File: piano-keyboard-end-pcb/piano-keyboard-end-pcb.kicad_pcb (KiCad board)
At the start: 2 copper layers, 41.1 x 82 mm, 24 parts, among them J1 Conn_01x03_Male, J2 Conn_01x01_Male, J3 Conn_01x02_Male, J4 Conn_01x02_Male, J5 Conn_01x05_Female, J6 AudioJack2, SW1 SW_Push, SW2 SW_Push, SW3 SW_Push, SW4 SW_Push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

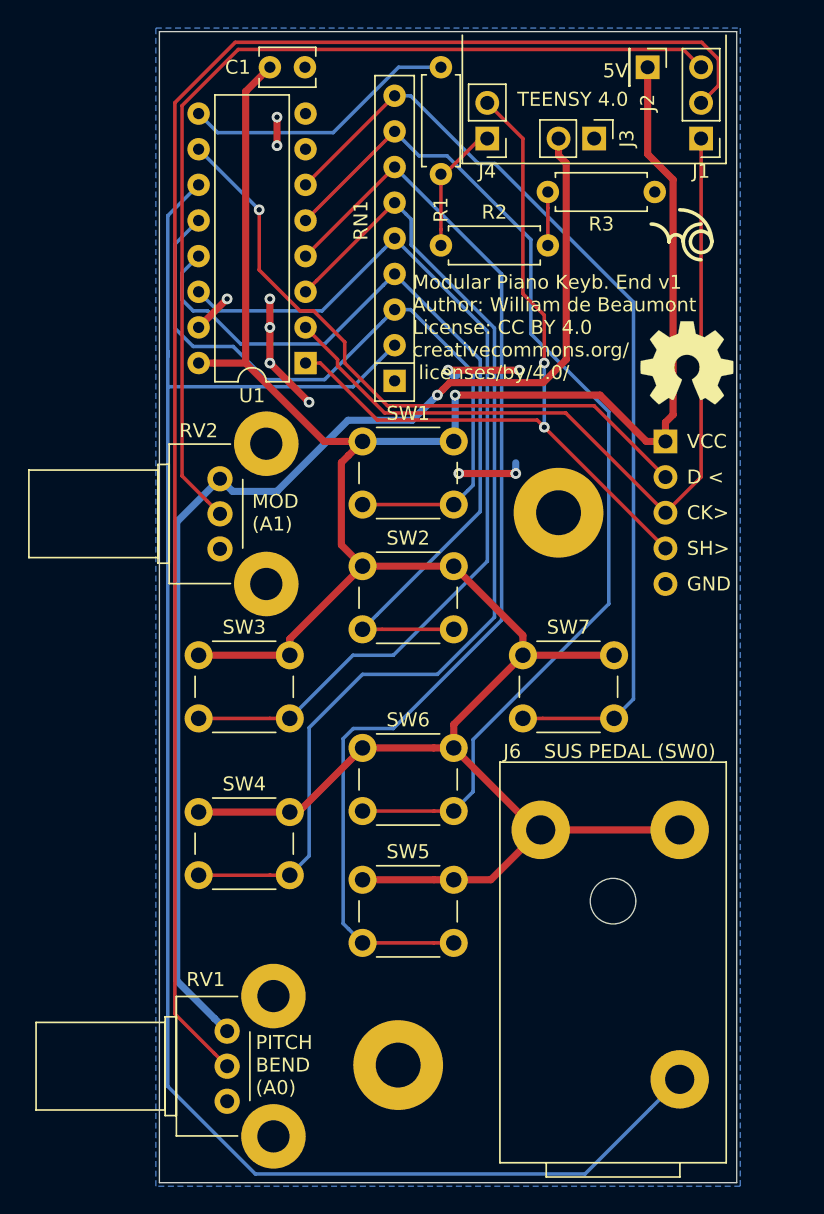
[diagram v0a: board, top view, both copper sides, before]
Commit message: move mod pot right so it aligns with edge and pitch bend pot
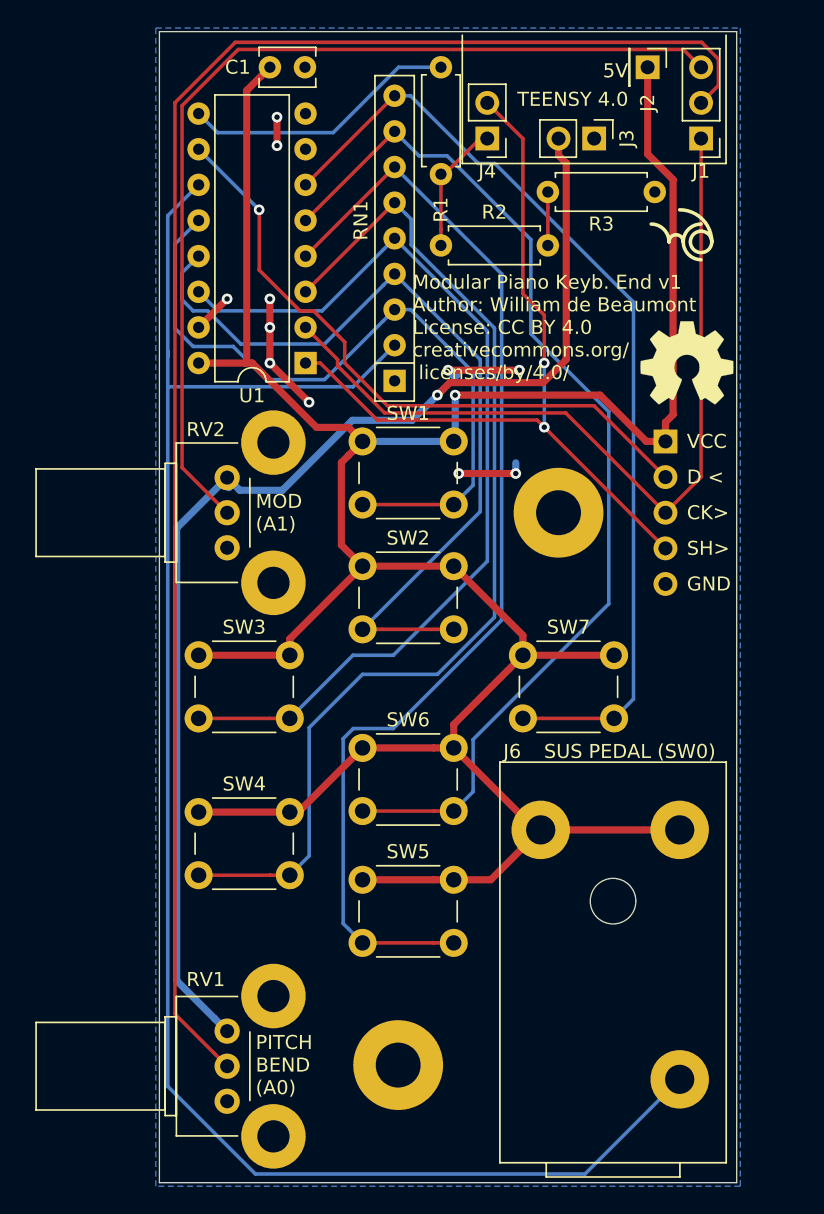
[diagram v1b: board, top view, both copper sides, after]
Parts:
- moved RV2 0.52 mm to (79.2, 68.6)
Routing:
- net +3V3: track 87.1 -> 87.7 mm
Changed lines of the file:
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@@
     (thickness 1.6)
     (drawings 23)
-    (tracks 233)
+    (tracks 236)
     (zones 0)
     (modules 24)
@@
   )
   (module Potentiometer_THT:Potentiometer_Bourns_PTV09A-2_Single_Horizontal (layer F.Cu)
-    (at 78.74 68.7 180)
+    (at 79.25 68.62 180)
     (descr "Potentiometer, horizontal, Bourns PTV09A-2 Single, http://www.bourns.com/docs/Product-Datasheets/ptv09.pdf")
     (tags "Potentiometer horizontal Bourns PTV09A-2 Single")
@@
     (effects (font (size 1 1) (thickness 0.15)) (justify left))
   )
-  (gr_text "MOD\n(A1)" (at 81.026 71.12) (layer F.SilkS)
+  (gr_text "MOD\n(A1)" (at 81.28 71.12) (layer F.SilkS)
     (effects (font (size 1 1) (thickness 0.15)) (justify left))
   )
@@
   (segment (start 82.296 57.912) (end 82.296 55.88) (width 0.508) (layer F.Cu) (net 1))
   (segment (start 95.4 66.04) (end 88.9 66.04) (width 0.508) (layer B.Cu) (net 2))
-  (segment (start 78.34737 60.452) (end 77.216 60.452) (width 0.508) (layer F.Cu) (net 2))
-  (segment (start 80.567842 60.452) (end 78.34737 60.452) (width 0.508) (layer F.Cu) (net 2))
-  (segment (start 86.155842 66.04) (end 80.567842 60.452) (width 0.508) (layer F.Cu) (net 2))
-  (segment (start 88.9 66.04) (end 86.155842 66.04) (width 0.508) (layer F.Cu) (net 2))
-  (segment (start 80.567842 41.098158) (end 82.296 39.37) (width 0.508) (layer F.Cu) (net 2))
-  (segment (start 80.567842 60.452) (end 80.567842 41.098158) (width 0.508) (layer F.Cu) (net 2))
   (segment (start 100.33 81.28) (end 106.83 81.28) (width 0.508) (layer F.Cu) (net 2))
   (segment (start 95.4 86.21) (end 100.33 81.28) (width 0.508) (layer F.Cu) (net 2))
@@
   (segment (start 109.22 45.562158) (end 111.036001 47.378159) (width 0.508) (layer F.Cu) (net 2))
   (segment (start 109.22 39.37) (end 109.22 45.562158) (width 0.508) (layer F.Cu) (net 2))
-  (segment (start 77.840001 70.300001) (end 78.74 71.2) (width 0.254) (layer F.Cu) (net 3))
-  (segment (start 76.034999 68.494999) (end 77.840001 70.300001) (width 0.254) (layer F.Cu) (net 3))
-  (segment (start 76.034999 42.105119) (end 76.034999 68.494999) (width 0.254) (layer F.Cu) (net 3))
+  (segment (start 78.34737 60.452) (end 77.216 60.452) (width 0.508) (layer F.Cu) (net 2))
+  (segment (start 85.625843 65.040001) (end 81.037842 60.452) (width 0.508) (layer F.Cu) (net 2))
+  (segment (start 87.900001 65.040001) (end 85.625843 65.040001) (width 0.508) (layer F.Cu) (net 2))
+  (segment (start 88.9 66.04) (end 87.900001 65.040001) (width 0.508) (layer F.Cu) (net 2))
+  (segment (start 80.644999 41.021001) (end 80.644999 60.325001) (width 0.508) (layer F.Cu) (net 2))
+  (segment (start 80.644999 60.325001) (end 80.518 60.452) (width 0.508) (layer F.Cu) (net 2))
+  (segment (start 82.296 39.37) (end 80.644999 41.021001) (width 0.508) (layer F.Cu) (net 2))
+  (segment (start 81.037842 60.452) (end 80.518 60.452) (width 0.508) (layer F.Cu) (net 2))
+  (segment (start 80.518 60.452) (end 78.34737 60.452) (width 0.508) (layer F.Cu) (net 2))
   (segment (start 111.76 38.1) (end 80.040118 38.1) (width 0.254) (layer F.Cu) (net 3))
   (segment (start 80.040118 38.1) (end 76.034999 42.105119) (width 0.254) (layer F.Cu) (net 3))
   (segment (start 113.03 39.37) (end 111.76 38.1) (width 0.254) (layer F.Cu) (net 3))
+  (segment (start 76.034999 67.904999) (end 79.25 71.12) (width 0.254) (layer F.Cu) (net 3))
+  (segment (start 76.034999 42.105119) (end 76.034999 67.904999) (width 0.254) (layer F.Cu) (net 3))
   (segment (start 75.526989 106.846989) (end 78.350001 109.670001) (width 0.254) (layer F.Cu) (net 4))
   (segment (start 75.526989 41.894695) (end 75.526989 106.846989) (width 0.254) (layer F.Cu) (net 4))
@@
   (segment (start 103.378 64.008) (end 110.49 71.12) (width 0.254) (layer F.Cu) (net 5))
   (segment (start 90.467764 64.008) (end 103.378 64.008) (width 0.254) (layer F.Cu) (net 5))
-  (segment (start 79.639999 69.599999) (end 78.74 68.7) (width 0.508) (layer B.Cu) (net 6))
-  (segment (start 87.863843 64.531999) (end 82.795843 69.599999) (width 0.508) (layer B.Cu) (net 6))
-  (segment (start 82.795843 69.599999) (end 79.639999 69.599999) (width 0.508) (layer B.Cu) (net 6))
-  (segment (start 75.653991 104.473991) (end 78.350001 107.170001) (width 0.508) (layer B.Cu) (net 6))
-  (segment (start 78.350001 107.170001) (end 79.25 108.07) (width 0.508) (layer B.Cu) (net 6))
-  (segment (start 75.653991 71.786009) (end 75.653991 104.473991) (width 0.508) (layer B.Cu) (net 6))
-  (segment (start 78.74 68.7) (end 75.653991 71.786009) (width 0.508) (layer B.Cu) (net 6))
   (via (at 94.234 62.738) (size 0.762) (drill 0.381) (layers F.Cu B.Cu) (net 6))
   (segment (start 94.218001 62.753999) (end 94.234 62.738) (width 0.508) (layer B.Cu) (net 6))
@@
   (segment (start 95.123001 61.848999) (end 94.614999 62.357001) (width 0.508) (layer F.Cu) (net 6))
   (segment (start 101.772723 61.848999) (end 95.123001 61.848999) (width 0.508) (layer F.Cu) (net 6))
-  (segment (start 92.440001 64.531999) (end 94.234 62.738) (width 0.508) (layer B.Cu) (net 6))
-  (segment (start 87.863843 64.531999) (end 92.440001 64.531999) (width 0.508) (layer B.Cu) (net 6))
   (segment (start 103.416001 60.205721) (end 101.772723 61.848999) (width 0.508) (layer F.Cu) (net 6))
   (segment (start 103.416001 46.198082) (end 103.416001 60.205721) (width 0.508) (layer F.Cu) (net 6))
   (segment (start 102.87 45.652081) (end 103.416001 46.198082) (width 0.508) (layer F.Cu) (net 6))
   (segment (start 102.87 44.45) (end 102.87 45.652081) (width 0.508) (layer F.Cu) (net 6))
+  (segment (start 78.350001 107.170001) (end 79.25 108.07) (width 0.508) (layer B.Cu) (net 6))
+  (segment (start 75.653991 104.473991) (end 78.350001 107.170001) (width 0.508) (layer B.Cu) (net 6))
+  (segment (start 79.382 69.342) (end 78.74 68.7) (width 0.508) (layer B.Cu) (net 6))
+  (segment (start 94.234 62.738) (end 92.440001 64.531999) (width 0.508) (layer B.Cu) (net 6))
+  (segment (start 75.653991 72.216009) (end 75.653991 104.473991) (width 0.508) (layer B.Cu) (net 6))
+  (segment (start 79.25 68.62) (end 75.653991 72.216009) (width 0.508) (layer B.Cu) (net 6))
+  (segment (start 80.149999 69.519999) (end 79.25 68.62) (width 0.508) (layer B.Cu) (net 6))
+  (segment (start 83.188159 69.519999) (end 80.149999 69.519999) (width 0.508) (layer B.Cu) (net 6))
+  (segment (start 88.176159 64.531999) (end 83.188159 69.519999) (width 0.508) (layer B.Cu) (net 6))
+  (segment (start 92.440001 64.531999) (end 88.176159 64.531999) (width 0.508) (layer B.Cu) (net 6))
   (segment (start 100.33 44.45) (end 97.79 41.91) (width 0.254) (layer F.Cu) (net 7))
   (segment (start 89.95401 64.51601) (end 85.89 60.452) (width 0.254) (layer F.Cu) (net 7))

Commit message: move pitch bend pot up slightly to align with 10mil grid
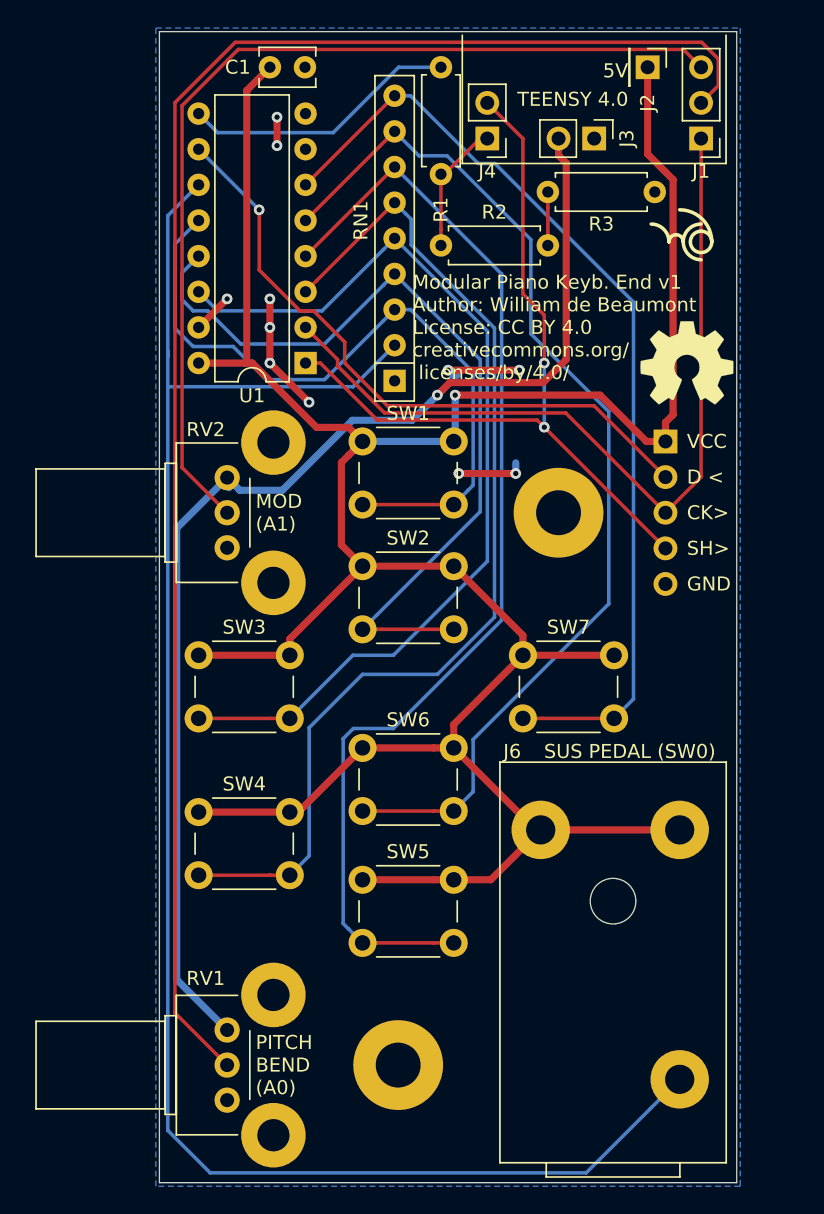
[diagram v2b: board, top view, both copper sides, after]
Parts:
- moved RV1 0.08 mm to (79.2, 108.0)
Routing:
- net Net-(J6-PadS): track 124.8 -> 126.6 mm
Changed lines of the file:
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@@
     (thickness 1.6)
     (drawings 23)
-    (tracks 236)
+    (tracks 234)
     (zones 0)
     (modules 24)
@@
   )
   (module Potentiometer_THT:Potentiometer_Bourns_PTV09A-2_Single_Horizontal (layer F.Cu)
-    (at 79.25 108.07 180)
+    (at 79.248 107.99 180)
     (descr "Potentiometer, horizontal, Bourns PTV09A-2 Single, http://www.bourns.com/docs/Product-Datasheets/ptv09.pdf")
     (tags "Potentiometer horizontal Bourns PTV09A-2 Single")
@@
   (segment (start 76.034999 67.904999) (end 79.25 71.12) (width 0.254) (layer F.Cu) (net 3))
   (segment (start 76.034999 42.105119) (end 76.034999 67.904999) (width 0.254) (layer F.Cu) (net 3))
-  (segment (start 75.526989 106.846989) (end 78.350001 109.670001) (width 0.254) (layer F.Cu) (net 4))
-  (segment (start 75.526989 41.894695) (end 75.526989 106.846989) (width 0.254) (layer F.Cu) (net 4))
   (segment (start 79.829693 37.591991) (end 75.526989 41.894695) (width 0.254) (layer F.Cu) (net 4))
   (segment (start 113.073873 37.591991) (end 79.829693 37.591991) (width 0.254) (layer F.Cu) (net 4))
-  (segment (start 78.350001 109.670001) (end 79.25 110.57) (width 0.254) (layer F.Cu) (net 4))
   (segment (start 114.261001 38.779119) (end 113.073873 37.591991) (width 0.254) (layer F.Cu) (net 4))
   (segment (start 114.261001 40.678999) (end 114.261001 38.779119) (width 0.254) (layer F.Cu) (net 4))
   (segment (start 113.03 41.91) (end 114.261001 40.678999) (width 0.254) (layer F.Cu) (net 4))
+  (segment (start 75.526989 106.768989) (end 79.248 110.49) (width 0.254) (layer F.Cu) (net 4))
+  (segment (start 75.526989 41.894695) (end 75.526989 106.768989) (width 0.254) (layer F.Cu) (net 4))
   (segment (start 113.03 68.58) (end 113.03 44.45) (width 0.254) (layer F.Cu) (net 5))
   (segment (start 110.49 71.12) (end 113.03 68.58) (width 0.254) (layer F.Cu) (net 5))
@@
   (segment (start 102.87 45.652081) (end 103.416001 46.198082) (width 0.508) (layer F.Cu) (net 6))
   (segment (start 102.87 44.45) (end 102.87 45.652081) (width 0.508) (layer F.Cu) (net 6))
-  (segment (start 78.350001 107.170001) (end 79.25 108.07) (width 0.508) (layer B.Cu) (net 6))
-  (segment (start 75.653991 104.473991) (end 78.350001 107.170001) (width 0.508) (layer B.Cu) (net 6))
   (segment (start 79.382 69.342) (end 78.74 68.7) (width 0.508) (layer B.Cu) (net 6))
   (segment (start 94.234 62.738) (end 92.440001 64.531999) (width 0.508) (layer B.Cu) (net 6))
-  (segment (start 75.653991 72.216009) (end 75.653991 104.473991) (width 0.508) (layer B.Cu) (net 6))
   (segment (start 79.25 68.62) (end 75.653991 72.216009) (width 0.508) (layer B.Cu) (net 6))
   (segment (start 80.149999 69.519999) (end 79.25 68.62) (width 0.508) (layer B.Cu) (net 6))
@@
   (segment (start 88.176159 64.531999) (end 83.188159 69.519999) (width 0.508) (layer B.Cu) (net 6))
   (segment (start 92.440001 64.531999) (end 88.176159 64.531999) (width 0.508) (layer B.Cu) (net 6))
+  (segment (start 75.653991 104.395991) (end 79.248 107.99) (width 0.508) (layer B.Cu) (net 6))
+  (segment (start 75.653991 72.216009) (end 75.653991 104.395991) (width 0.508) (layer B.Cu) (net 6))
   (segment (start 100.33 44.45) (end 97.79 41.91) (width 0.254) (layer F.Cu) (net 7))
   (segment (start 89.95401 64.51601) (end 85.89 60.452) (width 0.254) (layer F.Cu) (net 7))
@@
   (segment (start 95.4 70.54) (end 88.9 70.54) (width 0.254) (layer F.Cu) (net 18))
   (segment (start 77.216 47.752) (end 75.018981 49.949019) (width 0.254) (layer B.Cu) (net 19))
-  (segment (start 81.263119 118.251001) (end 104.760999 118.251001) (width 0.254) (layer B.Cu) (net 19))
-  (segment (start 75.018981 112.006863) (end 81.263119 118.251001) (width 0.254) (layer B.Cu) (net 19))
   (segment (start 75.018981 49.949019) (end 75.018981 59.601019) (width 0.254) (layer B.Cu) (net 19))
-  (segment (start 109.423201 113.588799) (end 111.506 111.506) (width 0.254) (layer B.Cu) (net 19))
-  (segment (start 104.760999 118.251001) (end 109.423201 113.588799) (width 0.254) (layer B.Cu) (net 19))
   (segment (start 75.018981 59.601019) (end 75.018981 60.002863) (width 0.254) (layer B.Cu) (net 19))
   (segment (start 75.01899 62.14101) (end 75.018981 62.141019) (width 0.254) (layer B.Cu) (net 19))
@@
   (segment (start 91.186 59.182) (end 88.22699 62.14101) (width 0.254) (layer B.Cu) (net 19))
   (segment (start 75.018981 59.601019) (end 75.018981 62.141019) (width 0.254) (layer B.Cu) (net 19))
-  (segment (start 75.018981 62.141019) (end 75.018981 112.006863) (width 0.254) (layer B.Cu) (net 19))
+  (segment (start 109.423201 113.588799) (end 111.506 111.506) (width 0.254) (layer B.Cu) (net 19))
+  (segment (start 104.840999 118.171001) (end 109.423201 113.588799) (width 0.254) (layer B.Cu) (net 19))
+  (segment (start 78.039001 118.171001) (end 104.840999 118.171001) (width 0.254) (layer B.Cu) (net 19))
+  (segment (start 75.018981 115.150981) (end 78.039001 118.171001) (width 0.254) (layer B.Cu) (net 19))
+  (segment (start 75.018981 62.141019) (end 75.018981 115.150981) (width 0.254) (layer B.Cu) (net 19))
   (zone (net 1) (net_name GND) (layer B.Cu) (hatch edge 0.508)
     (connect_pads (clearance 0.508))
